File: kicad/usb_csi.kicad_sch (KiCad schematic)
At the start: 32 parts, among them J1 USB_C One, J2 USB_C Two, J3 USB Programmer, SW1 SW_Push, SW2 SW_SPDT, SW3 SW_Push, U1 STM32F103R8Tx

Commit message: Added decoupling caps
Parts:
- removed BT1: Battery_Cell, symbol Device:Battery_Cell
- added C1: 4.7uF, symbol Device:C_Small
- added C2, C3, C4, C5, C6: 100nF, symbol Device:C_Small
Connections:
- net +3.3VP: now also U1.13 (VDDA), U1.19 (VDD), U1.32 (VDD), U1.48 (VDD), U1.64 (VDD), C1.1, C2.1, C3.1, C4.1, C5.1, C6.1
- net GND: now also D20.1 (K), D21.1 (K), SW1.2, U1.12 (VSSA), U1.18 (VSS), U1.31 (VSS), U1.47 (VSS), U1.63 (VSS), C1.2, C2.2, C3.2, C4.2, C5.2, C6.2
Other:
- moved on the sheet: D20, D21

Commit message: Viva la resistance
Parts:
- added R10, R11, R12, R13, R14, R15, R16, R17, R18, R19, R20, R21, R22, R23, R24, R4, R5, R6, R7, R8, R9: 300ohm, symbol Device:R
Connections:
- net at D21.2 (A): now also R24.2; no longer U1.6 (PD1)
- net at D2.2 (A): now also R5.1; no longer U1.9 (PC1)
- net at D10.2 (A): now also R13.1; no longer U1.40 (PC9)
- net at D19.2 (A): now also R22.1; no longer U1.34 (PB13)
- net at D6.2 (A): now also R9.1; no longer U1.25 (PC5)
- net at D4.2 (A): now also R7.1; no longer U1.11 (PC3)
- net at D7.2 (A): now also R10.1; no longer U1.37 (PC6)
- net at D5.2 (A): now also R8.1; no longer U1.24 (PC4)
- net at D11.2 (A): now also R14.1; no longer U1.51 (PC10)
- net at D17.2 (A): now also R20.1; no longer U1.36 (PB15)
- net at D12.2 (A): now also R15.1; no longer U1.52 (PC11)
- net at D15.2 (A): now also R18.1; no longer U1.3 (PC14)
- net at D9.2 (A): now also R12.1; no longer U1.39 (PC8)
- net at D3.2 (A): now also R6.1; no longer U1.10 (PC2)
- net at U1.2 (PC13): now also R17.2; no longer D14.2 (A)
- net at U1.35 (PB14): now also R21.2; no longer D18.2 (A)
- net at U1.38 (PC7): now also R11.2; no longer D8.2 (A)
- net at U1.4 (PC15): now also R19.2; no longer D16.2 (A)
- net at U1.5 (PD0): now also R23.1; no longer D20.2 (A)
- net at U1.53 (PC12): now also R16.2; no longer D13.2 (A)
- net at D1.2 (A): now also R4.1; no longer U1.8 (PC0)
- new net: R4.2, U1.8 (PC0)
- new net: R18.2, U1.3 (PC14)
- new net: R12.2, U1.39 (PC8)
- new net: R20.2, U1.36 (PB15)
- new net: R8.2, U1.24 (PC4)
- new net: R13.2, U1.40 (PC9)
- new net: D20.2 (A), R23.2
- new net: R6.2, U1.10 (PC2)
- new net: R7.2, U1.11 (PC3)
- new net: R9.2, U1.25 (PC5)
- new net: R22.2, U1.34 (PB13)
- new net: R10.2, U1.37 (PC6)
- new net: R14.2, U1.51 (PC10)
- new net: R15.2, U1.52 (PC11)
- new net: R24.1, U1.6 (PD1)
- new net: R5.2, U1.9 (PC1)
- new net: D8.2 (A), R11.1
- new net: D13.2 (A), R16.1
- new net: D14.2 (A), R17.1
- new net: D16.2 (A), R19.1
- new net: D18.2 (A), R21.1
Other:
- moved on the sheet: D1, D10, D11, D12, D13, D14, D15, D16, D17, D18, D19, D2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

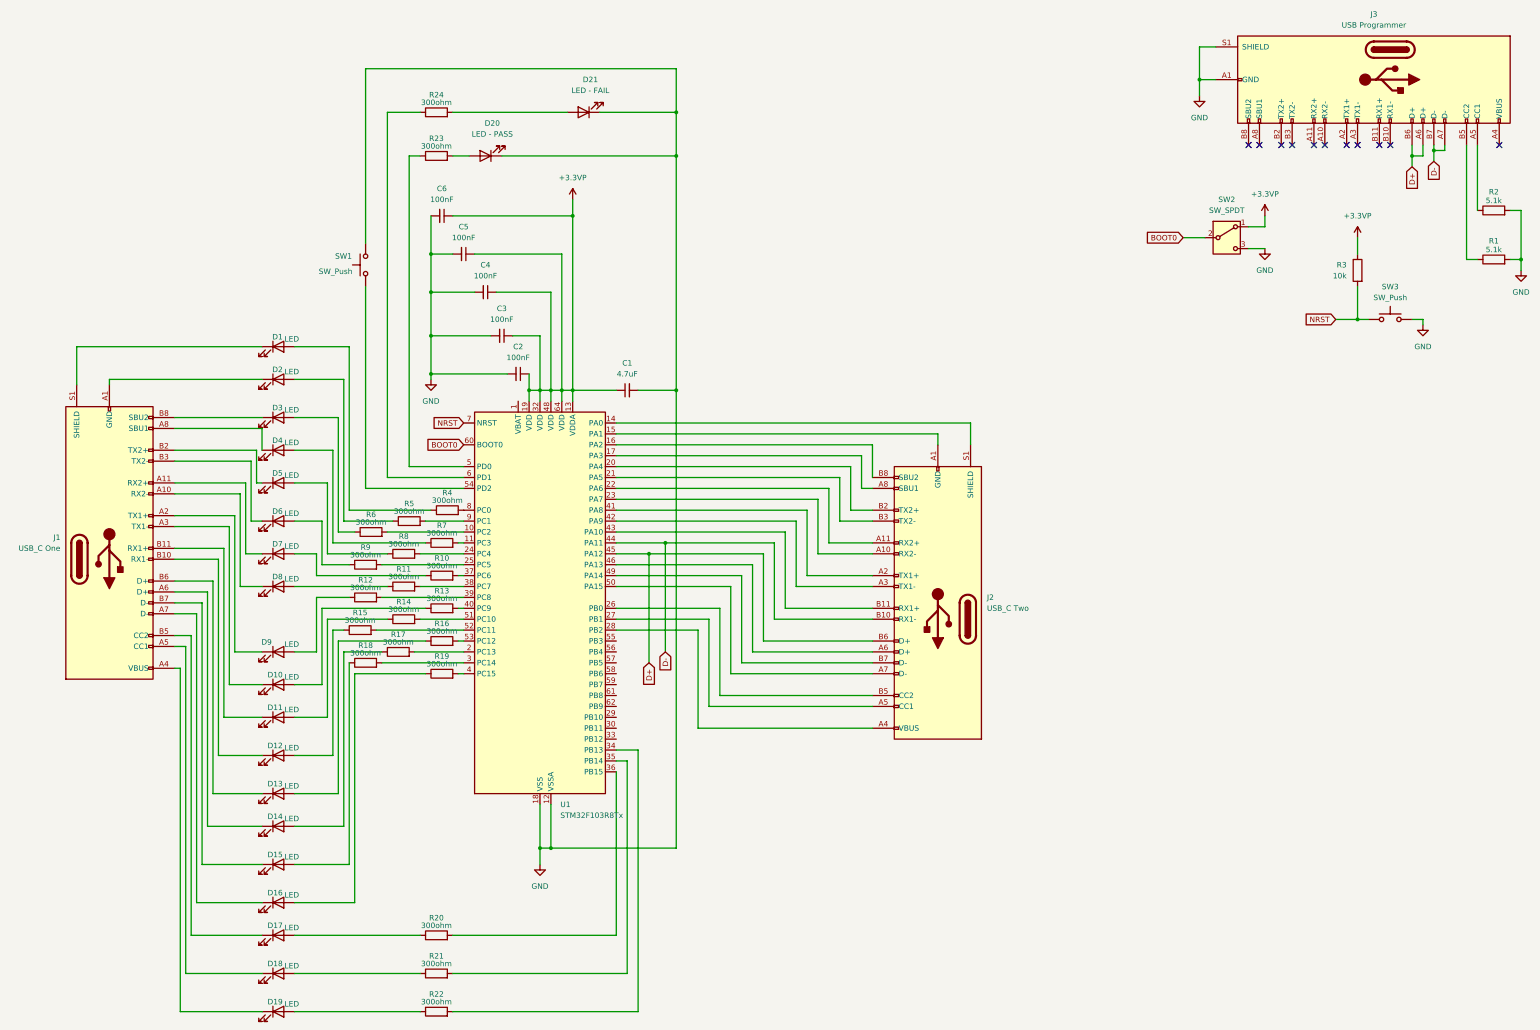
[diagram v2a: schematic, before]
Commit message: Adding connections for stlink programming, and disabling the USB based programming connections, since this particular stm32 does not have USB programming. We need to use something newer link STM32L433RC for that feature.
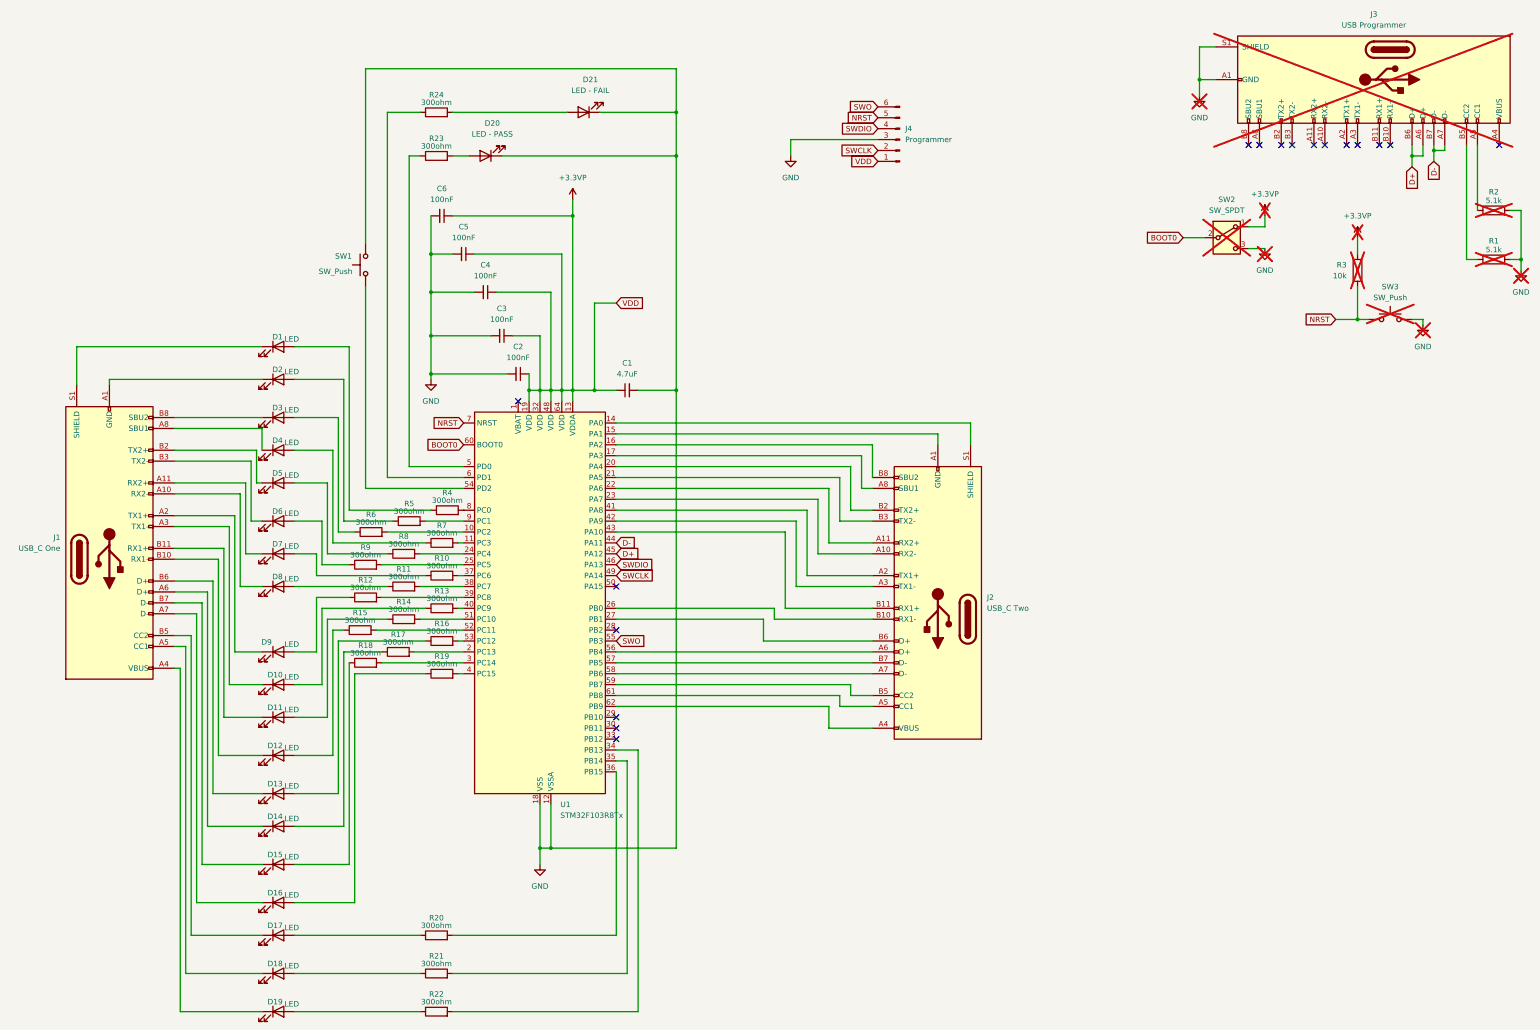
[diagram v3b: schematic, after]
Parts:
- added J4: Programmer, symbol Connector:Conn_01x06_Pin
- J3, R1, R2, R3, SW2, SW3: now not fitted; now left out of the parts list
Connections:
- net +3.3VP: now also J4.1 (Pin_1)
- net D+: no longer J2.B6 (D+)
- net D-: no longer J2.B10 (RX1-)
- net GND: now also J4.3 (Pin_3)
- net NRST: now also J4.5 (Pin_5)
- net at U1.26 (PB0): now also J2.B10 (RX1-); no longer J2.B5 (CC2)
- net at U1.27 (PB1): now also J2.B6 (D+); no longer J2.A5 (CC1)
- net at J2.A4 (VBUS), J2.A9 (VBUS), J2.B4 (VBUS)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: now also U1.62 (PB9); no longer U1.28 (PB2)
- net at J2.A6 (D+): now also U1.56 (PB4); no longer U1.46 (PA13)
- net at J2.B7 (D-): now also U1.57 (PB5); no longer U1.49 (PA14)
- net at U1.50 (PA15): no longer J2.A7 (D-)
- net SWO: now reaches U1.55 (PB3)
- net SWO: now also J4.6 (Pin_6)
- net at U1.58 (PB6): now also J2.A7 (D-)
- net at U1.59 (PB7): now also J2.B5 (CC2)
- net at U1.61 (PB8): now also J2.A5 (CC1)
- new net SWCLK: J4.2 (Pin_2), U1.49 (PA14)
- new net SWDIO: J4.4 (Pin_4), U1.46 (PA13)
- no-connect marks 11 -> 17
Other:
- title: USB_CSI -> USB_C CableMaster5000

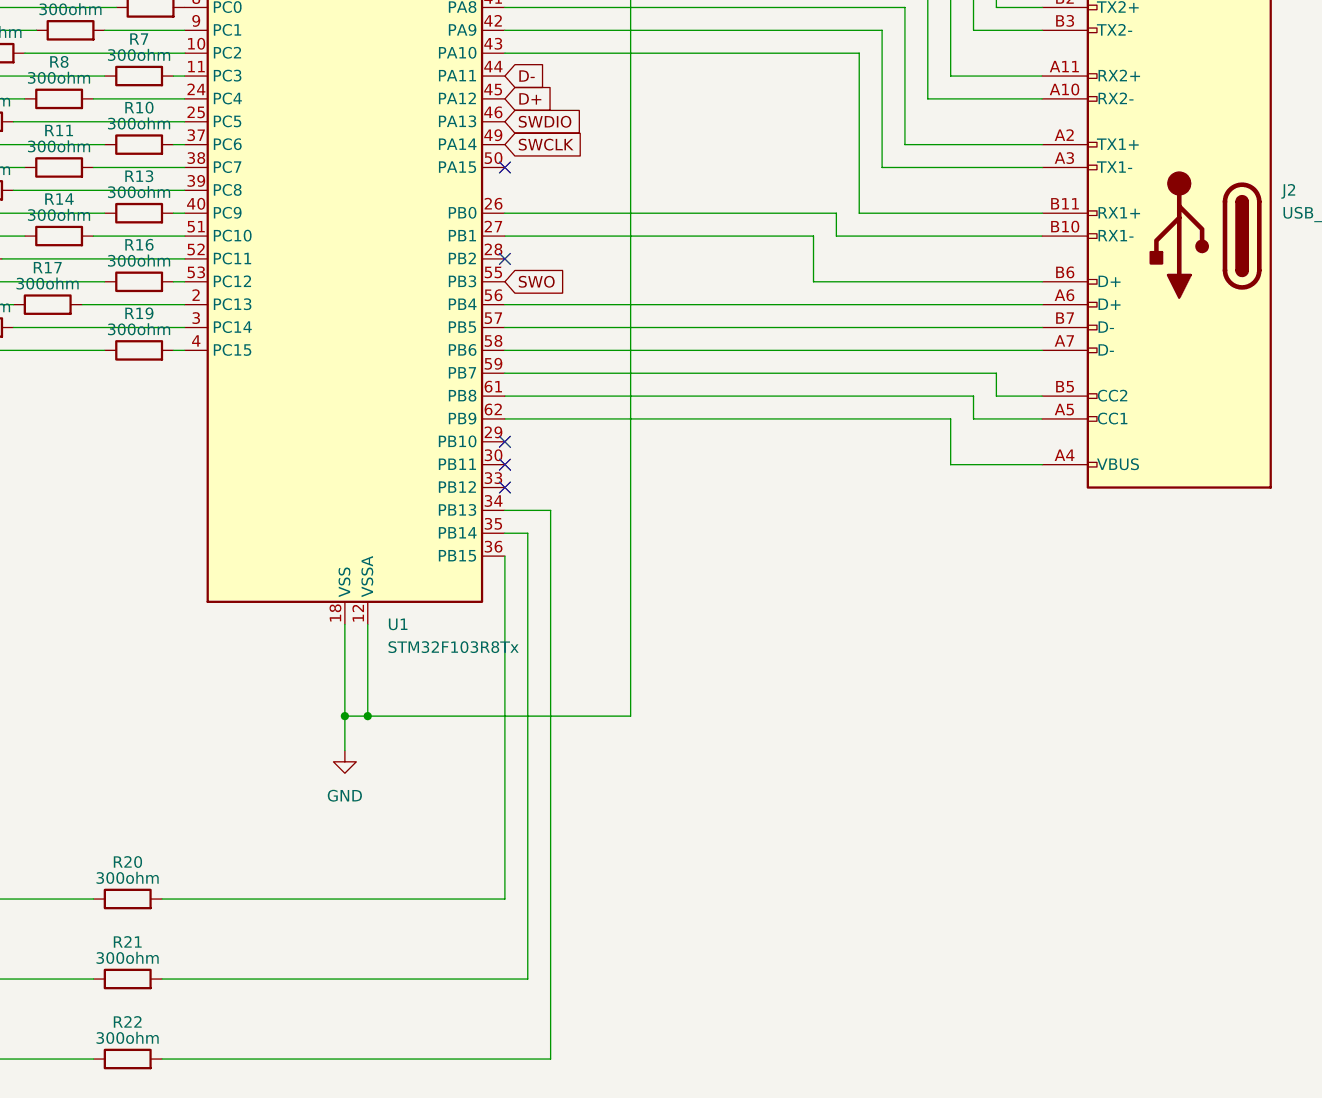
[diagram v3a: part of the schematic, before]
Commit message: Adding connections for SPI
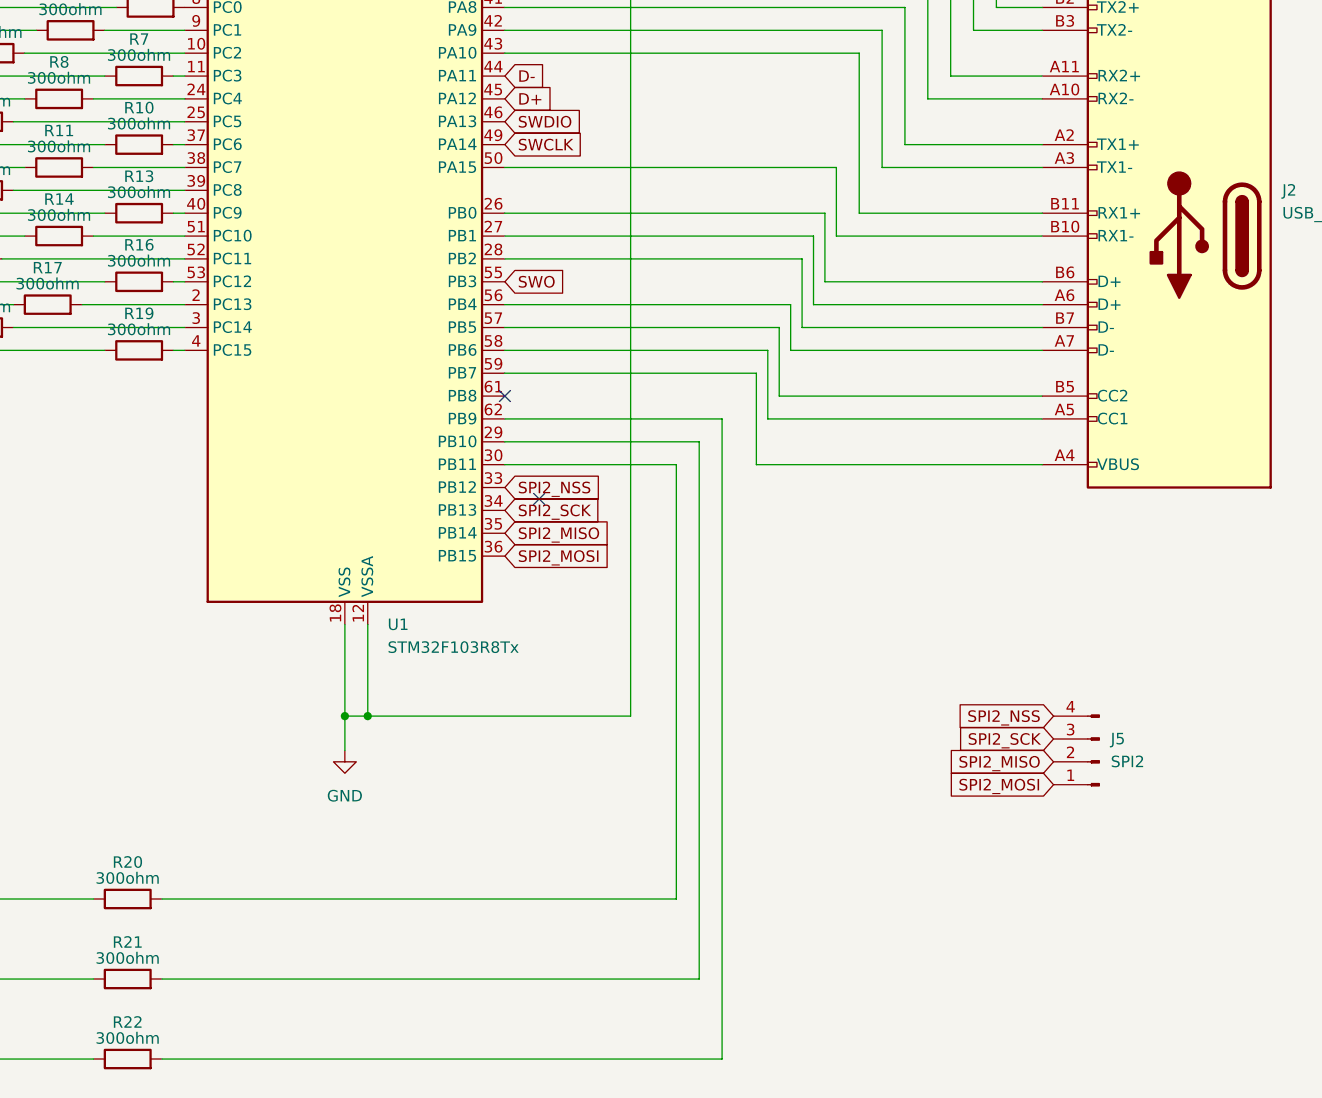
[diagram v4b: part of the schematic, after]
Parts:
- added J5: SPI2, symbol Connector:Conn_01x04_Pin
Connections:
- net at R20.2: now also U1.30 (PB11); no longer U1.36 (PB15)
- net at U1.26 (PB0): now also J2.B6 (D+); no longer J2.B10 (RX1-)
- net at U1.27 (PB1): now also J2.A6 (D+); no longer J2.B6 (D+)
- net at U1.28 (PB2): now also J2.B7 (D-)
- net at U1.29 (PB10): now also R21.2
- net SPI2_NSS: now reaches U1.33 (PB12)
- net SPI2_NSS: now also J5.4 (Pin_4)
- net at R22.2: now also U1.62 (PB9); no longer U1.34 (PB13)
- net SPI2_MISO: now reaches U1.35 (PB14)
- net SPI2_MISO: now also J5.2 (Pin_2); no longer R21.2
- net at U1.50 (PA15): now also J2.B10 (RX1-)
- net at U1.56 (PB4): now also J2.A7 (D-); no longer J2.A6 (D+)
- net at U1.57 (PB5): now also J2.B5 (CC2); no longer J2.B7 (D-)
- net at U1.58 (PB6): now also J2.A5 (CC1); no longer J2.A7 (D-)
- net at U1.59 (PB7): now also J2.A4 (VBUS), J2.A9 (VBUS), J2.B4 (VBUS), J2.B9 (VBUS); no longer J2.B5 (CC2)
- net at U1.61 (PB8): no longer J2.A5 (CC1)
- new net SPI2_MOSI: J5.1 (Pin_1), U1.36 (PB15)
- new net SPI2_SCK: J5.3 (Pin_3), U1.34 (PB13)
- no-connect marks 17 -> 14
